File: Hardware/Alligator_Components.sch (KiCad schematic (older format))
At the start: 122 parts, among them J1 SWD_Header, J2 Eurorack_10_pin_power, J3 Conn_01x08_Female, J4 Conn_01x08_Female, J5 Conn_01x08_Female, J6 Conn_01x08_Female, SW1 SW_SPST, SW2 SW_SPDT_MSM, U1 STM32H743ZITx, U2 IS42S16400J-xC, U3 PCM5100APW, U4 SSI2164, U5 MCP6004, U6 MCP6004, U7 TL074, U8 LM1117-3.3, Y1 8MHz 20pF

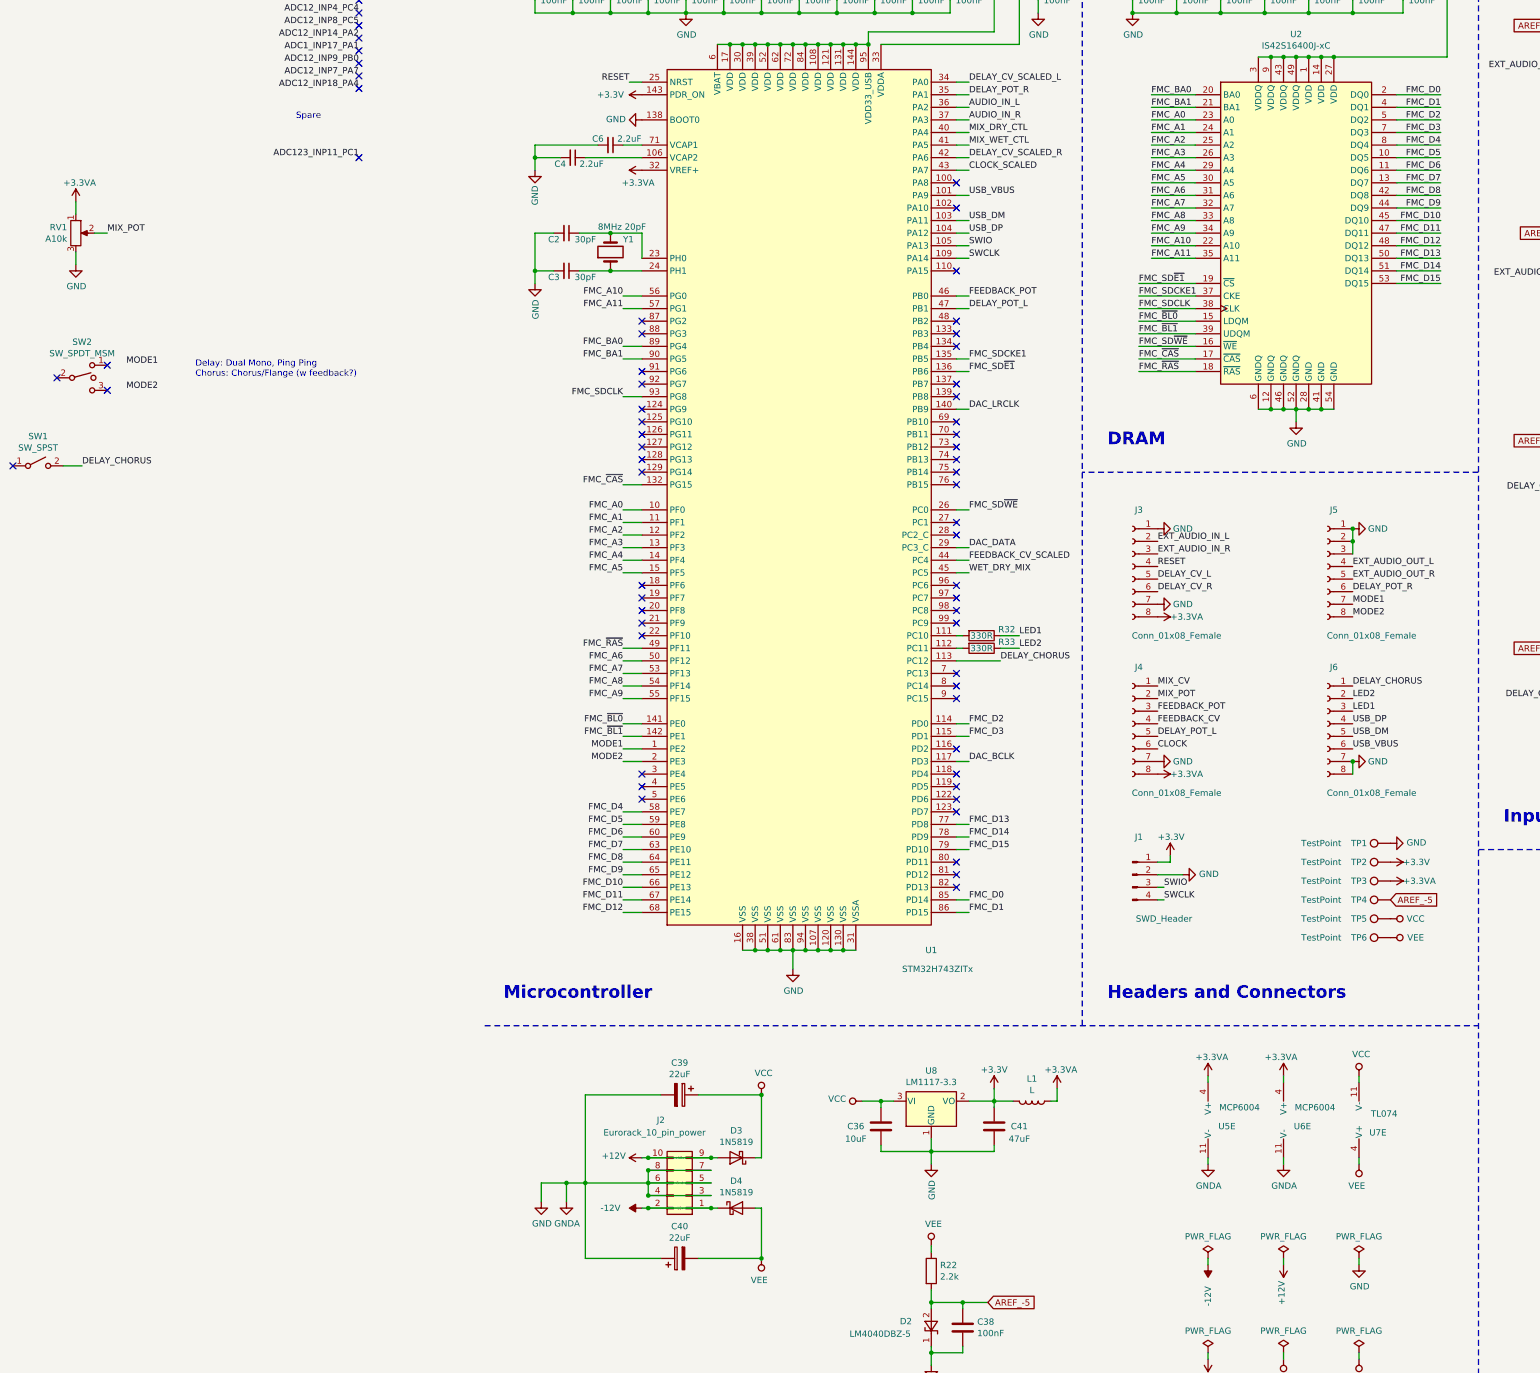
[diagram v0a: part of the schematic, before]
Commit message: Components first draft done; Started Controls PCB; Gerber and SMT assembly tests
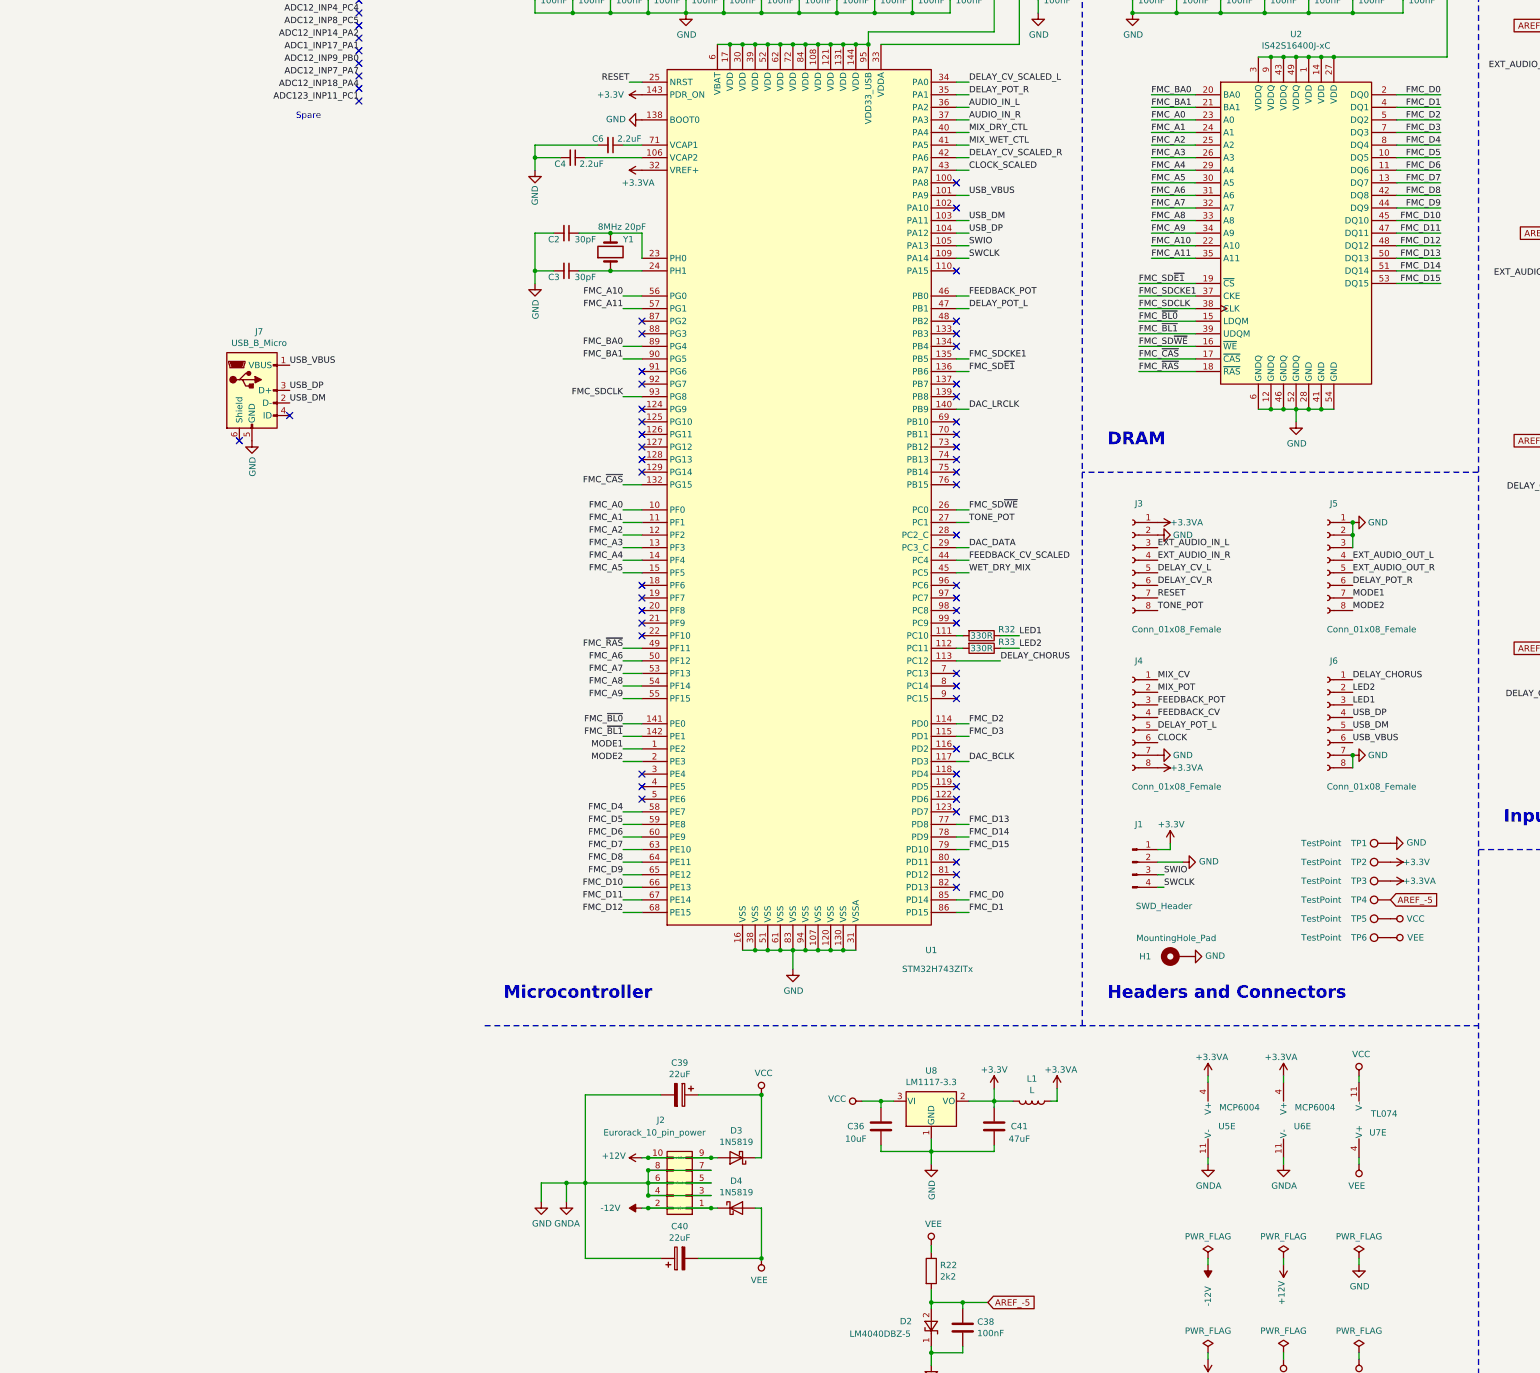
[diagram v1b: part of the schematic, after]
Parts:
- removed RV1: A10k, Resistors_SMD:R_0603_HandSoldering, symbol Device:R_POT
- removed SW1: SW_SPST, Resistors_SMD:R_0603_HandSoldering, symbol Switch:SW_SPST
- removed SW2: SW_SPDT_MSM, Resistors_SMD:R_0603_HandSoldering, symbol Switch:SW_SPDT_MSM
- added H1: MountingHole_Pad, Mounting_Holes:MountingHole_3.2mm_M3, symbol Mechanical:MountingHole_Pad
- added J7: USB_B_Micro, Custom_Footprints:USB_Micro-B_Amphenol, symbol Connector:USB_B_Micro
- C1, C10, C11, C12, C13, C14, C15, C16, C17, C19, C20, C21, C24, C25, C26, C35, C37, C38, C42, C44, C46, C5, C7, C8, C9: Part_Number (none) -> C14663
- C18, C23, C27, C28: Part_Number (none) -> C84721
- C2, C3: Part_Number (none) -> C22397
- C22, C43: Part_Number (none) -> C15850
- C29, C30, C32, C34, C45: Part_Number (none) -> C1595
- C31, C33, C4, C6: Part_Number (none) -> C49217
- C36: Part_Number (none) -> C249452
- C41: Part_Number (none) -> C134798
- C47, C48: Part_Number (none) -> C46653
- C49, C50, C51, C52: Part_Number (none) -> C1790
- D2: Part_Number (none) -> C69316
- D3, D4: Part_Number (none) -> C169540
- J3, J4, J5, J6: footprint Socket_Strips:Socket_Strip_Straight_1x08_Pitch2.54mm -> Pin_Headers:Pin_Header_Straight_1x08_Pitch2.54mm
- L1: Part_Number (none) -> C1046
- R1, R10, R14, R18, R19, R2: Part_Number (none) -> C22984
- R11: Part_Number (none) -> C23206
- R12, R13: Part_Number (none) -> C23212
- R15, R16, R17, R3: Part_Number (none) -> C23193
- R20, R21, R42, R43: Part_Number (none) -> C21190
- R22: value 2.2k -> 2k2; Part_Number (none) -> C4190
- R23, R25: Part_Number (none) -> C23231
- R24, R26, R5: Part_Number (none) -> C25803
- R27, R28, R31, R34, R7, R9: Part_Number (none) -> C25819
- R29: Part_Number (none) -> C23242
- R30, R4: Part_Number (none) -> C23265
- R32, R33: Part_Number (none) -> C23138
- R36, R37: Part_Number (none) -> C4190
- R38, R39: Part_Number (none) -> C25804
- R40, R41: Part_Number (none) -> C4216
- R6, R8: Part_Number (none) -> C4184
- U1: Part_Number (none) -> C114408
- U2: Part_Number (none) -> C69411
- U3: Part_Number (none) -> C131154
- U5, U6: Part_Number (none) -> C7378
- U7: Part_Number (none) -> C6964
- U8: Part_Number (none) -> C6186
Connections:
- net +3.3VA: now also J3.1 (Pin_1); no longer J3.8 (Pin_8)
- net EXT_AUDIO_IN_L: now also J3.3 (Pin_3); no longer J3.2 (Pin_2)
- net EXT_AUDIO_IN_R: now also J3.4 (Pin_4); no longer J3.3 (Pin_3)
- net GND: now also J3.2 (Pin_2), H1.1, J7.5 (GND); no longer J3.1 (Pin_1), J3.7 (Pin_7)
- net RESET: now also J3.7 (Pin_7); no longer J3.4 (Pin_4)
- net USB_DM: now also J7.2 (D-)
- net USB_DP: now also J7.3 (D+)
- net USB_VBUS: now also J7.1 (VBUS)
- net TONE_POT: now reaches U1.27 (PC1)
- net TONE_POT: now also J3.8 (Pin_8)
- no-connect marks 67 -> 64
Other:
- note removed: "Delay: Dual Mono, Ping Ping\nChorus: Chorus/Flange (w feedback?)"
- moved on the sheet: J1, J3, J4, J5, J6

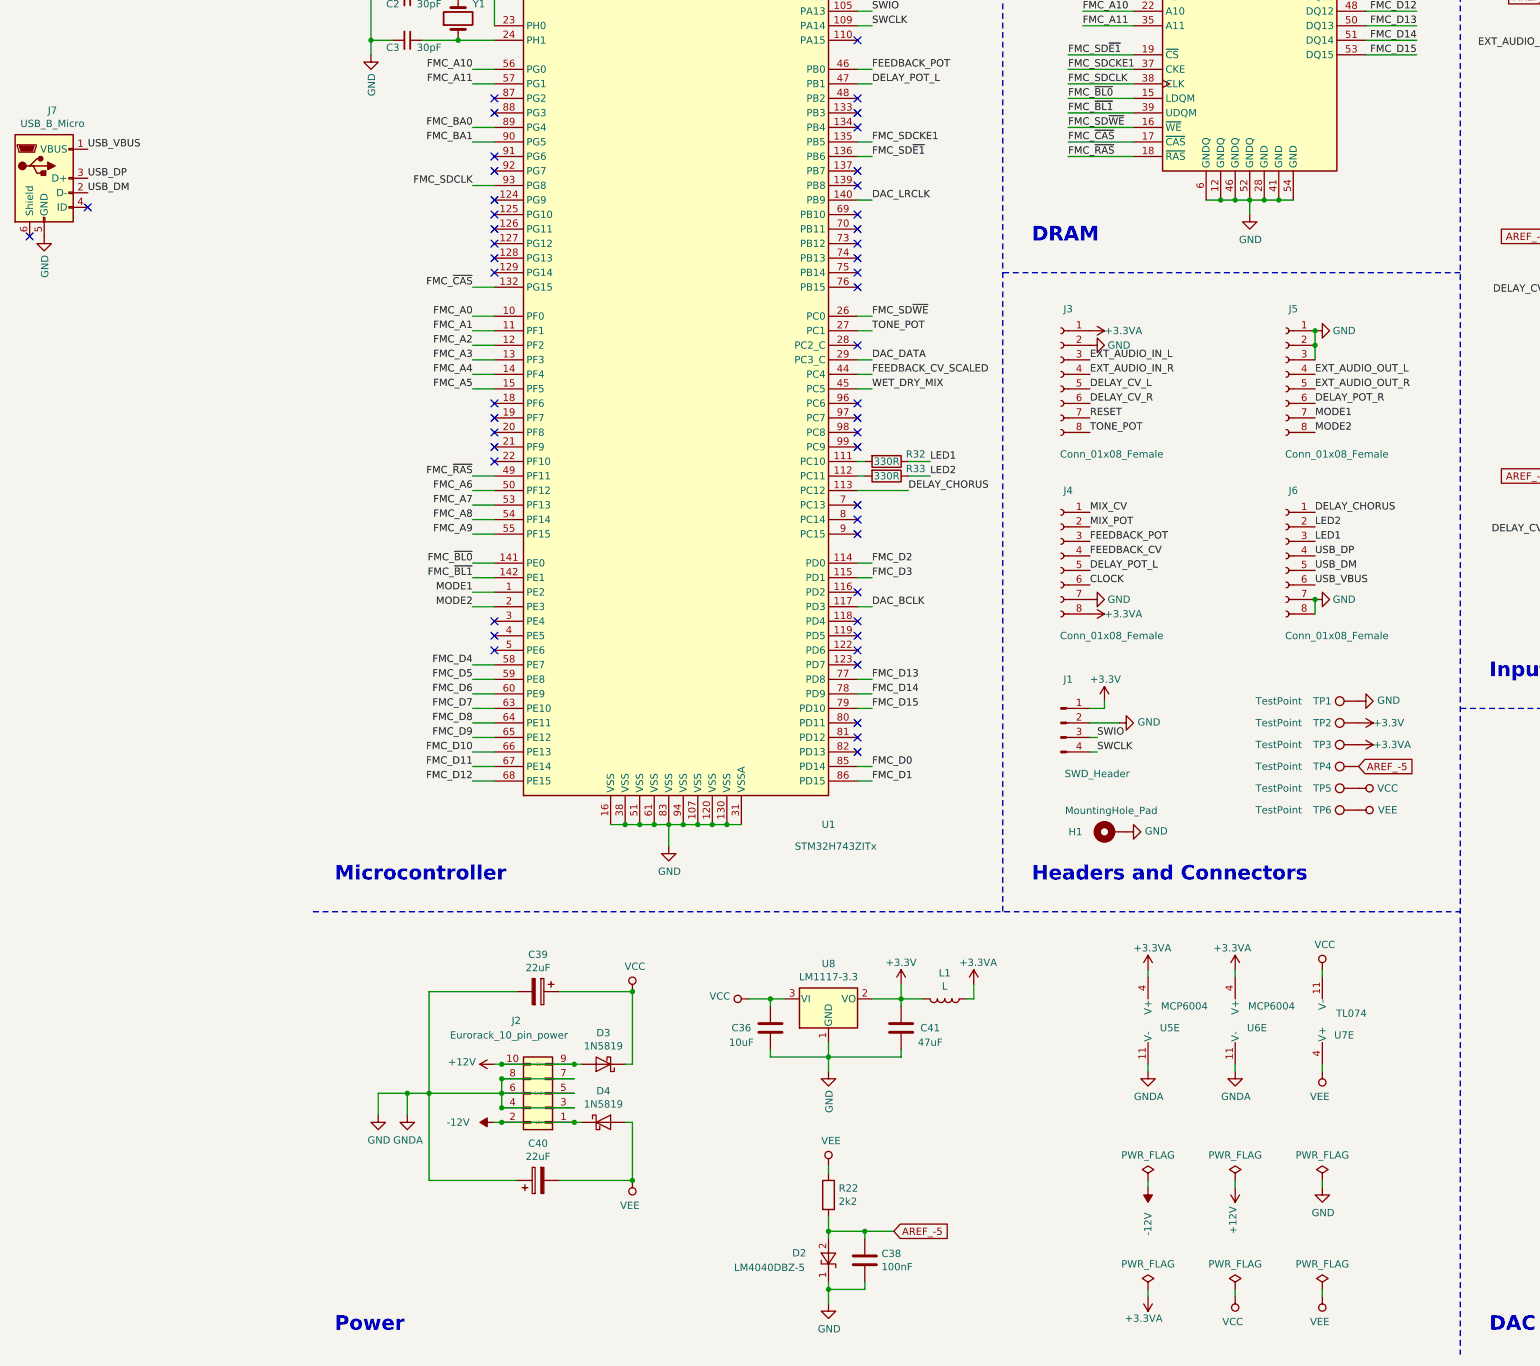
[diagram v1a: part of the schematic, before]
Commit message: Tooling holes added for SMT assembly; started routing control PCB
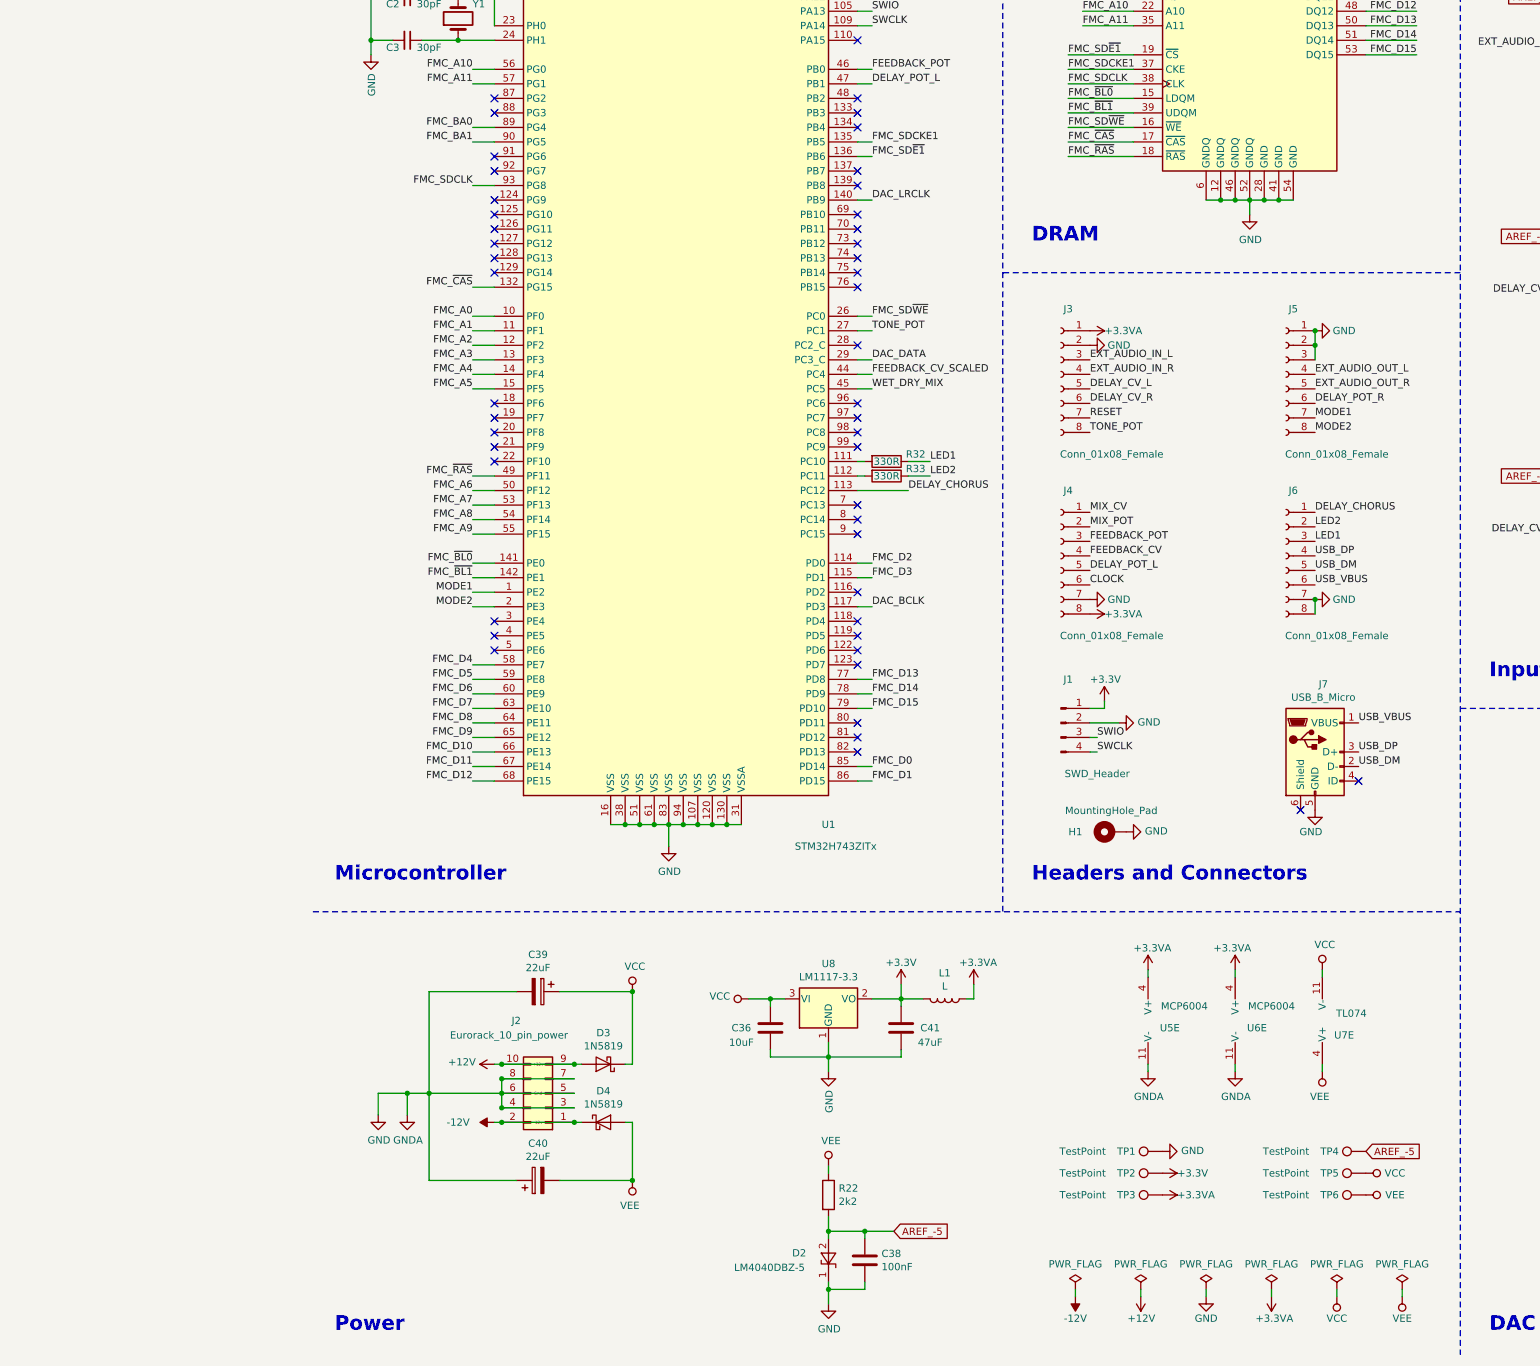
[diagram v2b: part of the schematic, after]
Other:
- moved on the sheet: J7, TP1, TP2, TP3, TP4, TP5, TP6

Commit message: Control PCB orientation tests
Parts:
- removed H1: MountingHole_Pad, Mounting_Holes:MountingHole_3.2mm_M3, symbol Mechanical:MountingHole_Pad
- added H1, H2: JLC_Tooling_Hole, Custom_Footprints:JLC_SMT_Tooling_Hole, symbol Mechanical:MountingHole
- J3, J4, J5, J6: value Conn_01x08_Female -> Conn_01x08_Male; symbol Connector:Conn_01x08_Female -> Connector:Conn_01x08_Male
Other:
- moved on the sheet: J1, U5E, U6E, U7E

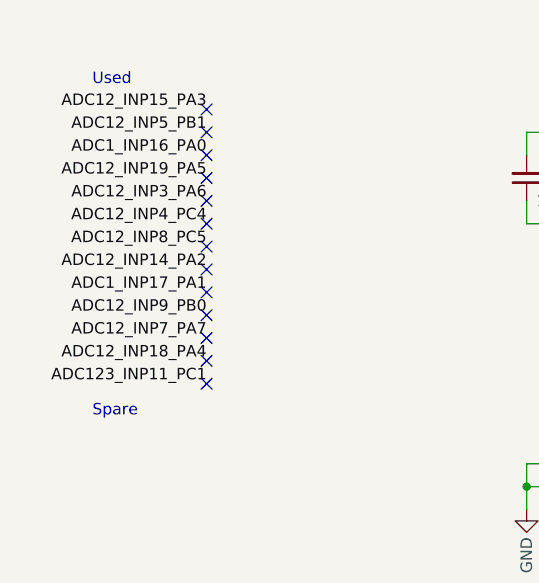
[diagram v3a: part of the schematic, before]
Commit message: Completed first draft of Panel PCB
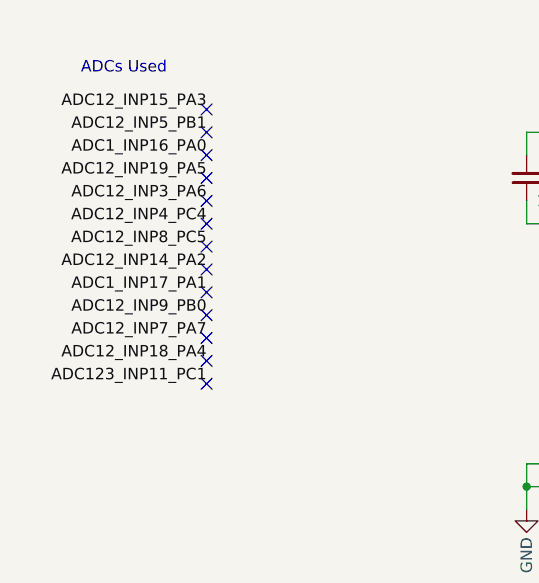
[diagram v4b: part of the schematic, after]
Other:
- note added: "ADCs Used"
- note removed: "Spare"
- note removed: "Used"
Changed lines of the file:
@@
 	1    0    0    -1
 $EndComp
-Text Notes -1000 800  0    50   ~ 0
-Used
+Text Notes -1050 750  0    50   ~ 0
+ADCs Used
 NoConn ~ -500 1000
 Text Label 4350 1950 0    50   ~ 0
@@
 Text Label 4350 2050 0    50   ~ 0
 DELAY_POT_R
-Text Notes -1000 2250 0    50   ~ 0
-Spare
 NoConn ~ -500 2000
 NoConn ~ -500 1900
